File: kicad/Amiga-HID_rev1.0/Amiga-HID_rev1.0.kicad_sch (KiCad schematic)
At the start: 58 parts, among them J1 USB-A Host, J2 JST-XH-5A, J3 OLED I2C, J4 Reserve 3V3+GP+GND+VSYS, J5 JST-SH-3 SWD, J6 JST-SH-3 UART, J7 Conn_01x06_Pin, SW1 SW_Push, SW2 SW_Push, U1 USBLC6-2SC6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

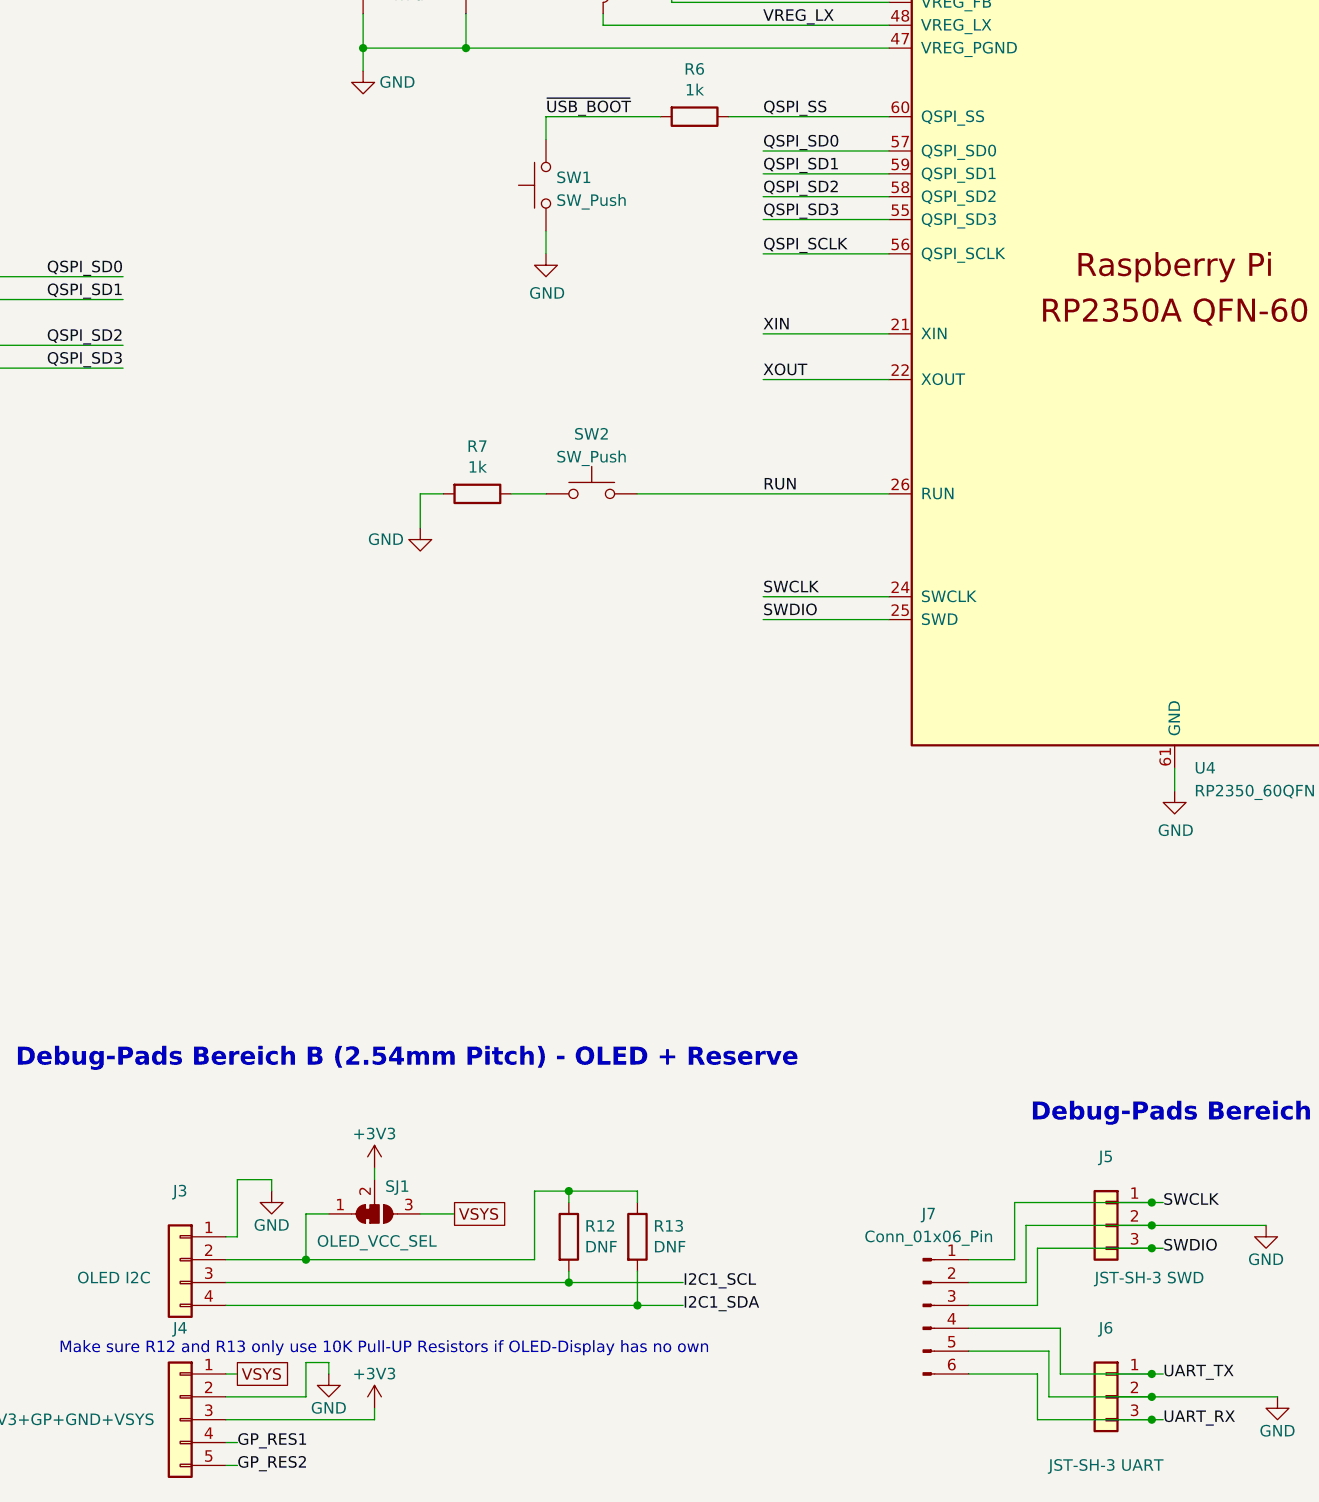
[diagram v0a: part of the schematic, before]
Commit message: Anordnung der Bauteile abgeschlossen
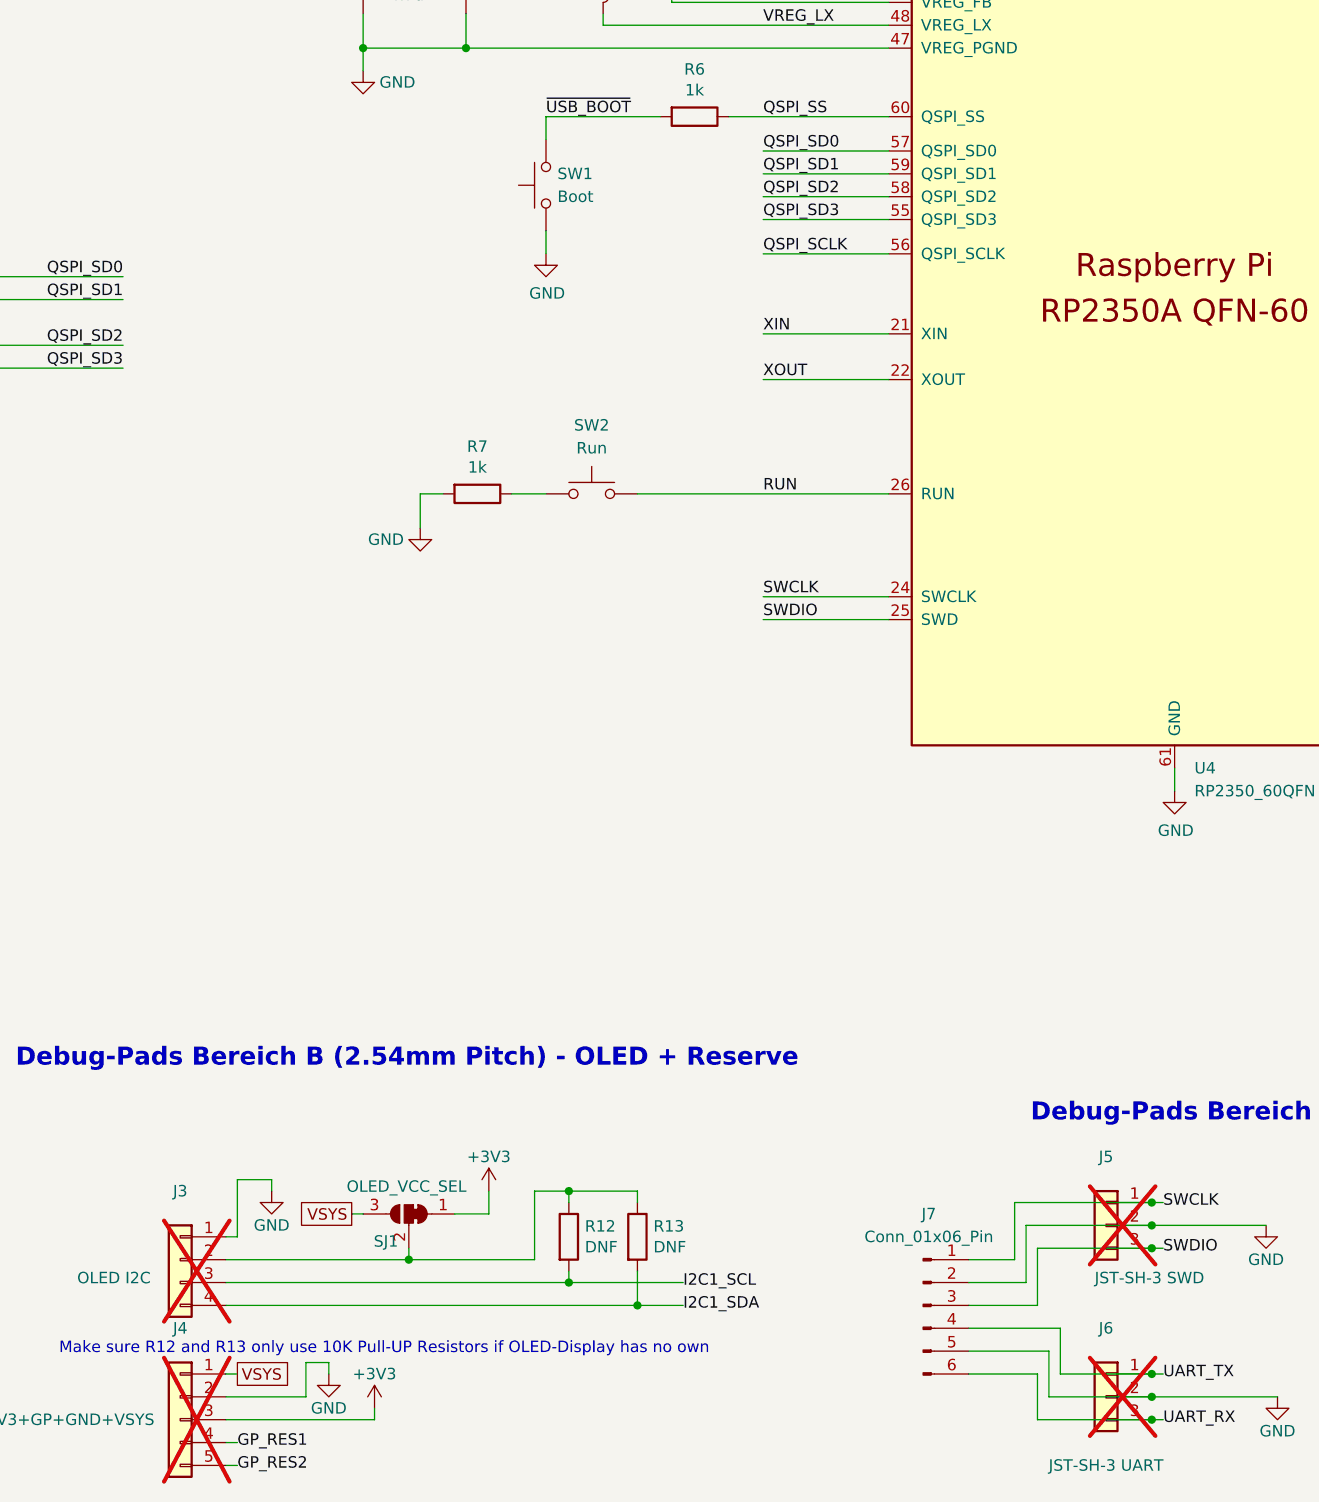
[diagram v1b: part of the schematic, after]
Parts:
- J3, J4, J5, J6: now not fitted
- LED2: GPIO (none) -> GP16
- SJ1: footprint Jumper:SolderJumper-3_P1.3mm_Open_Pad1.0x1.5mm -> Jumper:SolderJumper-3_P1.3mm_Bridged12_RoundedPad1.0x1.5mm
- SW1: value SW_Push -> Boot
- SW2: value SW_Push -> Run
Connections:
- net +3V3: now also SJ1.1 (A); no longer SJ1.2 (C)
- net at J3.2 (Pin_2), R12.1, R13.1: now also SJ1.2 (C); no longer SJ1.1 (A)
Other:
- moved on the sheet: SJ1
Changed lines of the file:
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@@
 	)
 	(junction
-		(at 121.92 254)
-		(diameter 0)
-		(color 0 0 0 0)
-	)
-	(junction
 		(at 139.7 119.38)
 		(diameter 0)
@@
 	)
 	(junction
+		(at 133.35 254)
+		(diameter 0)
+		(color 0 0 0 0)
+	)
+	(junction
 		(at 215.9 247.65)
 		(diameter 0)
@@
 	(wire
 		(pts
-			(xy 121.92 254) (xy 147.32 254)
-		)
-		(stroke
-			(width 0)
-			(type default)
-		)
-	)
-	(wire
-		(pts
 			(xy 250.19 189.23) (xy 265.43 189.23)
 		)
@@
 	(wire
 		(pts
-			(xy 121.92 248.92) (xy 124.46 248.92)
-		)
-		(stroke
-			(width 0)
-			(type default)
-		)
-	)
-	(wire
-		(pts
 			(xy 175.26 64.77) (xy 186.69 64.77)
 		)
@@
 	(wire
 		(pts
-			(xy 219.71 97.79) (xy 219.71 85.09)
+			(xy 133.35 254) (xy 147.32 254)
 		)
 		(stroke
@@
 	(wire
 		(pts
-			(xy 318.77 120.65) (xy 318.77 121.92)
+			(xy 219.71 97.79) (xy 219.71 85.09)
 		)
 		(stroke
@@
 	(wire
 		(pts
-			(xy 24.13 95.25) (xy 44.45 95.25)
+			(xy 318.77 120.65) (xy 318.77 121.92)
 		)
 		(stroke
@@
 	(wire
 		(pts
-			(xy 57.15 135.89) (xy 57.15 147.32)
+			(xy 24.13 95.25) (xy 44.45 95.25)
 		)
 		(stroke
@@
 	(wire
 		(pts
-			(xy 49.53 83.82) (xy 52.07 83.82)
+			(xy 57.15 135.89) (xy 57.15 147.32)
 		)
 		(stroke
@@
 	(wire
 		(pts
-			(xy 134.62 248.92) (xy 138.43 248.92)
+			(xy 49.53 83.82) (xy 52.07 83.82)
 		)
 		(stroke
@@
 	(wire
 		(pts
-			(xy 163.83 66.04) (xy 163.83 64.77)
+			(xy 142.24 248.92) (xy 142.24 246.38)
 		)
 		(stroke
@@
 	(wire
 		(pts
-			(xy 99.06 78.74) (xy 100.33 78.74)
+			(xy 163.83 66.04) (xy 163.83 64.77)
 		)
 		(stroke
@@
 	(wire
 		(pts
-			(xy 368.3 35.56) (xy 369.57 35.56)
+			(xy 99.06 78.74) (xy 100.33 78.74)
 		)
 		(stroke
@@
 	(wire
 		(pts
-			(xy 300.99 137.16) (xy 304.8 137.16)
+			(xy 368.3 35.56) (xy 369.57 35.56)
 		)
 		(stroke
@@
 	(wire
 		(pts
-			(xy 128.27 115.57) (xy 128.27 119.38)
+			(xy 300.99 137.16) (xy 304.8 137.16)
 		)
 		(stroke
@@
 	(wire
 		(pts
-			(xy 139.7 106.68) (xy 139.7 107.95)
+			(xy 128.27 115.57) (xy 128.27 119.38)
 		)
 		(stroke
@@
 	(wire
 		(pts
-			(xy 195.58 261.62) (xy 205.74 261.62)
+			(xy 139.7 106.68) (xy 139.7 107.95)
 		)
 		(stroke
@@
 	(wire
 		(pts
-			(xy 129.54 243.84) (xy 129.54 245.11)
+			(xy 195.58 261.62) (xy 205.74 261.62)
 		)
 		(stroke
@@
 	(wire
 		(pts
-			(xy 121.92 248.92) (xy 121.92 254)
-		)
-		(stroke
-			(width 0)
-			(type default)
-		)
-	)
-	(wire
-		(pts
 			(xy 311.15 120.65) (xy 311.15 121.92)
 		)
@@
 	(wire
 		(pts
+			(xy 133.35 252.73) (xy 133.35 254)
+		)
+		(stroke
+			(width 0)
+			(type default)
+		)
+	)
+	(wire
+		(pts
 			(xy 234.95 64.77) (xy 243.84 64.77)
 		)
@@
 	(wire
 		(pts
-			(xy 121.92 254) (xy 113.03 254)
+			(xy 113.03 254) (xy 133.35 254)
 		)
 		(stroke
@@
 	(wire
 		(pts
+			(xy 127 248.92) (xy 128.27 248.92)
+		)
+		(stroke
+			(width 0)
+			(type default)
+		)
+	)
+	(wire
+		(pts
 			(xy 250.19 105.41) (xy 256.54 105.41)
 		)
@@
 	(wire
 		(pts
+			(xy 138.43 248.92) (xy 142.24 248.92)
+		)
+		(stroke
+			(width 0)
+			(type default)
+		)
+	)
+	(wire
+		(pts
 			(xy 195.58 254) (xy 200.66 254)
 		)
@@
 	(global_label "VSYS"
 		(shape passive)
-		(at 138.43 248.92 0)
+		(at 127 248.92 180)
 		(fields_autoplaced yes)
 		(effects
@@
 				(size 1.27 1.27)
 			)
-			(justify left)
+			(justify right)
 		)
 		(property "Intersheetrefs" "${INTERSHEET_REFS}"
-			(at 138.43 248.92 0)
+			(at 120.5299 248.92 0)
 			(hide yes)
 			(show_name no)
@@
 		(on_board yes)
 		(in_pos_files yes)
-		(dnp no)
+		(dnp yes)
 		(property "Reference" "J5"
 			(at 210.82 242.57 0)
@@
 		(on_board yes)
 		(in_pos_files yes)
-		(dnp no)
+		(dnp yes)
 		(property "Reference" "J3"
 			(at 107.95 246.38 0)
@@
 		(fields_autoplaced yes)
 		(property "Reference" "SW2"
-			(at 153.67 162.2892 0)
+			(at 153.67 161.29 0)
 			(show_name no)
 			(do_not_autoplace no)
@@
 			)
 		)
-		(property "Value" "SW_Push"
-			(at 153.67 164.8261 0)
+		(property "Value" "Run"
+			(at 153.67 163.83 0)
 			(show_name no)
 			(do_not_autoplace no)
@@
 		(on_board yes)
 		(in_pos_files yes)
-		(dnp no)
+		(dnp yes)
 		(property "Reference" "J6"
 			(at 210.82 261.62 0)
@@
 	(symbol
 		(lib_id "power:+3V3")
-		(at 129.54 243.84 0)
+		(at 142.24 246.38 0)
 		(unit 1)
 		(body_style 1)
@@
 		(dnp no)
 		(property "Reference" "#PWR017"
-			(at 129.54 247.65 0)
+			(at 142.24 250.19 0)
 			(hide yes)
 			(show_name no)
@@
 		)
 		(property "Value" "+3V3"
-			(at 129.54 240.03 0)
+			(at 142.24 242.57 0)
 			(show_name no)
 			(do_not_autoplace no)
@@
 		)
 		(property "Footprint" ""
-			(at 129.54 243.84 0)
+			(at 142.24 246.38 0)
 			(hide yes)
 			(show_name no)
@@
 		)
 		(property "Datasheet" ""
-			(at 129.54 243.84 0)
+			(at 142.24 246.38 0)
 			(hide yes)
 			(show_name no)
@@
 		)
 		(property "Description" "Power symbol creates a global label with name \"+3V3\""
-			(at 129.54 243.84 0)
+			(at 142.24 246.38 0)
 			(hide yes)
 			(show_name no)
@@
 		(fields_autoplaced yes)
 		(property "Reference" "SW1"
-			(at 149.733 133.7853 90)
+			(at 149.86 133.3499 90)
 			(show_name no)
 			(do_not_autoplace no)
@@
 			)
 		)
-		(property "Value" "SW_Push"
-			(at 149.733 136.3222 90)
+		(property "Value" "Boot"
+			(at 149.86 135.8899 90)
 			(show_name no)
 			(do_not_autoplace no)
@@
 	(symbol
 		(lib_id "Jumper:SolderJumper_3_Bridged12")
-		(at 129.54 248.92 0)
-		(mirror x)
+		(at 133.35 248.92 0)
+		(mirror y)
 		(unit 1)
 		(body_style 1)
@@
 		(dnp no)
 		(property "Reference" "SJ1"
-			(at 132.08 245.872 0)
+			(at 130.81 251.968 0)
 			(show_name no)
 			(do_not_autoplace no)
@@
 		)
 		(property "Value" "OLED_VCC_SEL"
-			(at 129.794 251.968 0)
+			(at 133.096 245.872 0)
 			(show_name no)
 			(do_not_autoplace no)
@@
 			)
 		)
-		(property "Footprint" "Jumper:SolderJumper-3_P1.3mm_Open_Pad1.0x1.5mm"
-			(at 129.54 248.92 0)
+		(property "Footprint" "Jumper:SolderJumper-3_P1.3mm_Bridged12_RoundedPad1.0x1.5mm"
+			(at 133.35 248.92 0)
 			(hide yes)
 			(show_name no)
@@
 		)
 		(property "Datasheet" ""
-			(at 129.54 248.92 0)
+			(at 133.35 248.92 0)
 			(hide yes)
 			(show_name no)
@@
 		)
 		(property "Description" "3-pole Solder Jumper, pins 1+2 closed/bridged"
-			(at 129.54 248.92 0)
+			(at 133.35 248.92 0)
 			(hide yes)
 			(show_name no)
@@
 			)
 		)
+		(property "GPIO" "GP16"
+			(at 382.27 49.53 0)
+			(hide yes)
+			(show_name no)
+			(do_not_autoplace no)
+			(effects
+				(font
+					(size 1.27 1.27)
+				)
+			)
+		)
 		(pin "1"
 		)
@@
 		(on_board yes)
 		(in_pos_files yes)
-		(dnp no)
+		(dnp yes)
 		(property "Reference" "J4"
 			(at 107.95 261.62 0)

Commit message: fast fertig mit routing
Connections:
- net GND: no longer U1.2 (GND)
- net GPIO9: now also J4.5 (Pin_5)
- net USB_D+: now also U1.6 (I/O1); no longer U1.1 (I/O1)
- net USB_D-: now also U1.4 (I/O2); no longer U1.3 (I/O2)
- net USB_DM: now also U1.3 (I/O2); no longer U1.4 (I/O2)
- net USB_DP: now also U1.1 (I/O1); no longer U1.6 (I/O1)
- net GPIO7: now reaches J2.2 (Pin_2)
- net GPIO7: now also U4.10 (GPIO7)
- net GP_RES1 renamed GPIO8
- net GPIO8: now also U4.12 (GPIO8); no longer U4.10 (GPIO7)
- removed net GP_RES2: J4.5 (Pin_5), U4.12 (GPIO8)
- no-connect marks 21 -> 19
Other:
- moved on the sheet: D1, J1, U1
